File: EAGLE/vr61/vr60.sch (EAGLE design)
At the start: 228 parts, among them IC1 MC74VHC1G50, J6 MICROMOD-2222-C

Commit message: wip, logos
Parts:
- removed SG3: MOUNTING-HOLE-WIDE, ts_keyboards:MOUNTING-HOLE-WIDE
- added LOGO1: OSHW-LOGOL, random_logos:OSHW-LOGOL
- added U$5: SPARKFUN_LOGO0.2, random_logos:SPARKFUN_LOGO0.2
- SG1, SG4: value MOUNTING-HOLE-VWIDE -> MOUNTING-HOLE-VWIDEEDGE-CUT; device ts_keyboards:MOUNTING-HOLE-VWIDE -> ts_keyboards:MOUNTING-HOLE-VWIDEEDGE-CUT
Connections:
- removed net SG3: SG3.P$1
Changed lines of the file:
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@@
 <part name="U$3" library="ts_keyboards" deviceset="ESD_SRV05-4" device=""/>
 <part name="SC1" library="ts_keyboards" deviceset="MOUNTING-HOLE" device=""/>
-<part name="SG1" library="ts_keyboards" deviceset="MOUNTING-HOLE-VWIDE" device=""/>
 <part name="SC2" library="ts_keyboards" deviceset="MOUNTING-HOLE-WIDE" device=""/>
 <part name="U$7" library="ts_keyboards" deviceset="PTC_ASMD1206" device=""/>
@@
 <part name="X1" library="ts_keyboards" deviceset="USB_C" device=""/>
 <part name="GND3" library="ts_custom_nick_nacks" deviceset="GND" device=""/>
-<part name="SG4" library="ts_keyboards" deviceset="MOUNTING-HOLE-VWIDE" device=""/>
 <part name="SA1" library="ts_keyboards" deviceset="MOUNTING-HOLE-WIDE" device=""/>
-<part name="SG3" library="ts_keyboards" deviceset="MOUNTING-HOLE-WIDE" device=""/>
 <part name="SA3" library="ts_keyboards" deviceset="MOUNTING-HOLE-WIDE" device=""/>
 <part name="SA2" library="ts_keyboards" deviceset="MOUNTING-HOLE-WIDE" device=""/>
@@
 <part name="J4" library="SparkFun-Connectors" library_urn="urn:adsk.eagle:library:513" deviceset="CONN_03" device="" package3d_urn="urn:adsk.eagle:package:38063/1"/>
 <part name="U1" library="SparkFun-IC-Power" library_urn="urn:adsk.eagle:library:526" deviceset="V_REG_LM1117" device="SOT223" package3d_urn="urn:adsk.eagle:package:39069/1"/>
+<part name="SG1" library="ts_keyboards" deviceset="MOUNTING-HOLE-VWIDE" device="EDGE-CUT"/>
+<part name="SG4" library="ts_keyboards" deviceset="MOUNTING-HOLE-VWIDE" device="EDGE-CUT"/>
+<part name="LOGO1" library="random_logos" deviceset="OSHW-LOGO" device="L"/>
+<part name="U$5" library="random_logos" deviceset="SPARKFUN_LOGO" device="0.2"/>
 </parts>
 <sheets>
@@
 <instance part="U$3" gate="G$1" x="71.12" y="149.86" smashed="yes" rot="R90"/>
 <instance part="SC1" gate="G$1" x="233.68" y="33.02" smashed="yes"/>
-<instance part="SG1" gate="G$1" x="241.3" y="33.02" smashed="yes"/>
 <instance part="SC2" gate="G$1" x="236.22" y="33.02" smashed="yes"/>
 <instance part="U$7" gate="G$1" x="101.6" y="165.1" smashed="yes">
@@
 <attribute name="VALUE" x="170.18" y="3.048" size="1.778" layer="96" align="top-center"/>
 </instance>
-<instance part="SG4" gate="G$1" x="248.92" y="33.02" smashed="yes"/>
 <instance part="SA1" gate="G$1" x="254" y="33.02" smashed="yes"/>
-<instance part="SG3" gate="G$1" x="246.38" y="33.02" smashed="yes"/>
 <instance part="SA3" gate="G$1" x="259.08" y="33.02" smashed="yes"/>
 <instance part="SA2" gate="G$1" x="256.54" y="33.02" smashed="yes"/>
@@
 <attribute name="VALUE" x="88.9" y="53.34" size="1.778" layer="96" font="vector"/>
 </instance>
+<instance part="SG1" gate="G$1" x="241.3" y="35.56" smashed="yes"/>
+<instance part="SG4" gate="G$1" x="248.92" y="35.56" smashed="yes"/>
+<instance part="LOGO1" gate="G$1" x="210.82" y="22.86" smashed="yes"/>
+<instance part="U$5" gate="G$1" x="210.82" y="25.4" smashed="yes"/>
 </instances>
 <busses>
@@
 <segment>
 <label x="246.38" y="30.48" size="1.778" layer="95" rot="R270"/>
-<pinref part="SG3" gate="G$1" pin="P$1"/>
-<wire x1="246.38" y1="31.496" x2="246.38" y2="30.48" width="0.1524" layer="91"/>
+<wire x1="246.38" y1="34.036" x2="246.38" y2="30.48" width="0.1524" layer="91"/>
 </segment>
 </net>
@@
 <segment>
 <label x="241.3" y="30.48" size="1.778" layer="95" rot="R270"/>
+<wire x1="241.3" y1="34.036" x2="241.3" y2="30.48" width="0.1524" layer="91"/>
 <pinref part="SG1" gate="G$1" pin="P$1"/>
-<wire x1="241.3" y1="31.496" x2="241.3" y2="30.48" width="0.1524" layer="91"/>
 </segment>
 </net>
@@
 <segment>
 <label x="248.92" y="30.48" size="1.778" layer="95" rot="R270"/>
+<wire x1="248.92" y1="34.036" x2="248.92" y2="30.48" width="0.1524" layer="91"/>
 <pinref part="SG4" gate="G$1" pin="P$1"/>
-<wire x1="248.92" y1="31.496" x2="248.92" y2="30.48" width="0.1524" layer="91"/>
 </segment>
 </net>
 <net name="SG2" class="0">
 <segment>
-<wire x1="243.84" y1="30.48" x2="243.84" y2="33.02" width="0.1524" layer="91"/>
+<wire x1="243.84" y1="30.48" x2="243.84" y2="34.036" width="0.1524" layer="91"/>
 <label x="243.84" y="30.48" size="1.778" layer="95" rot="R270"/>
 </segment>

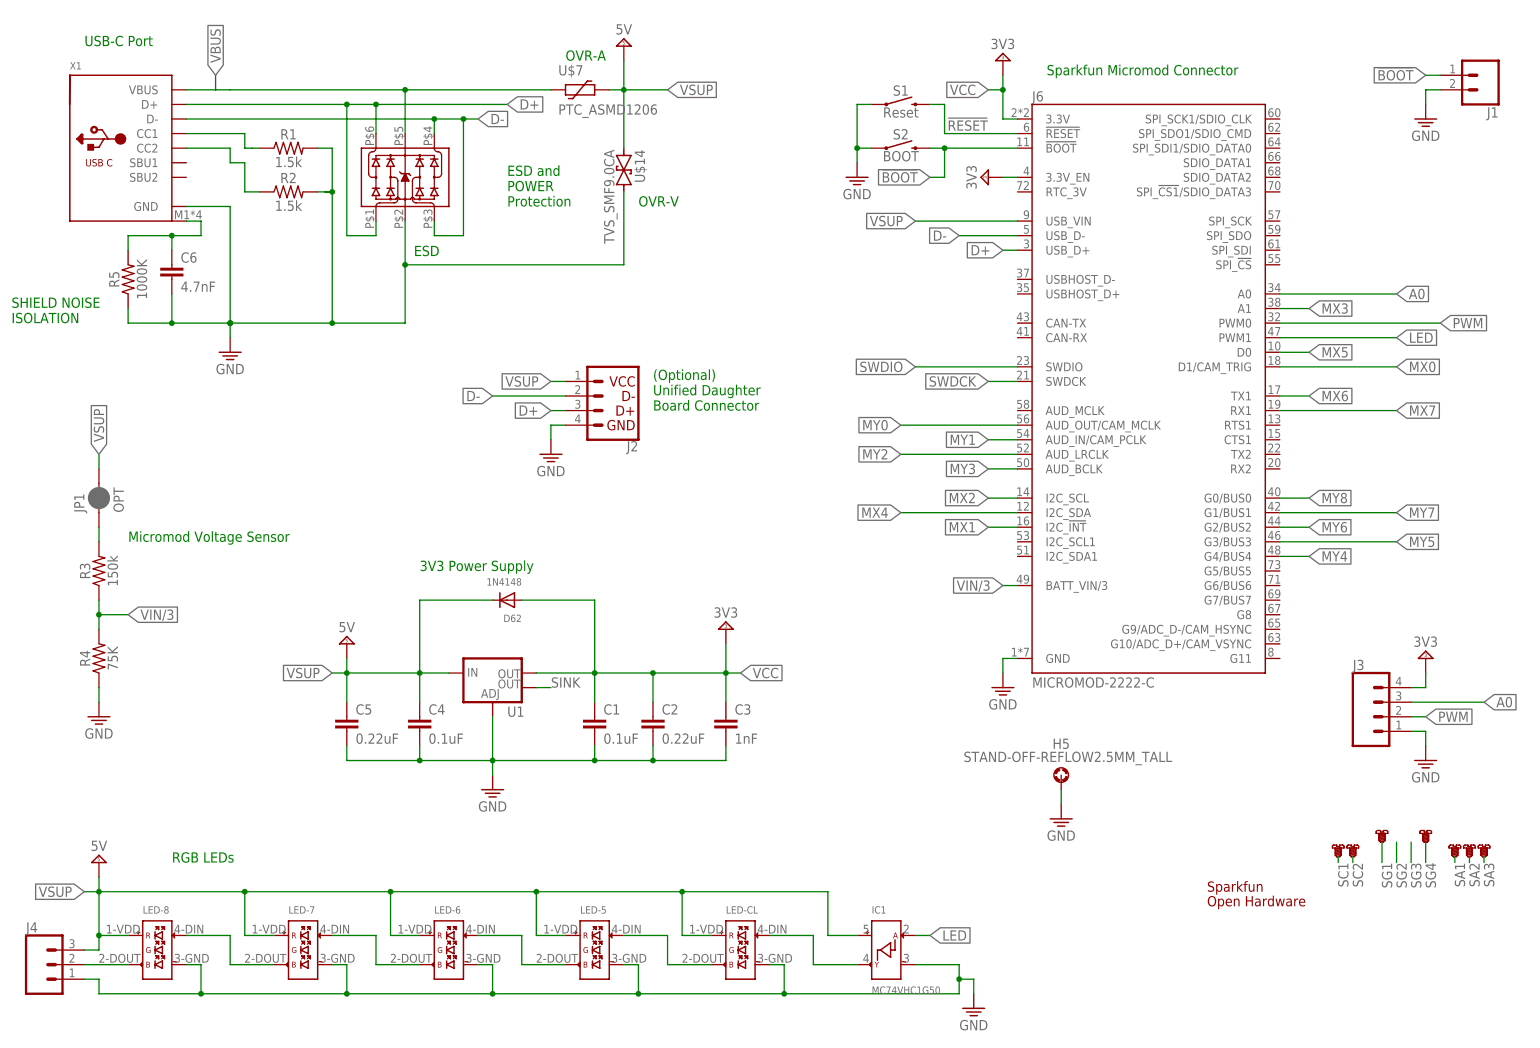
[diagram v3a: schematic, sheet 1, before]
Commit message: logos and text
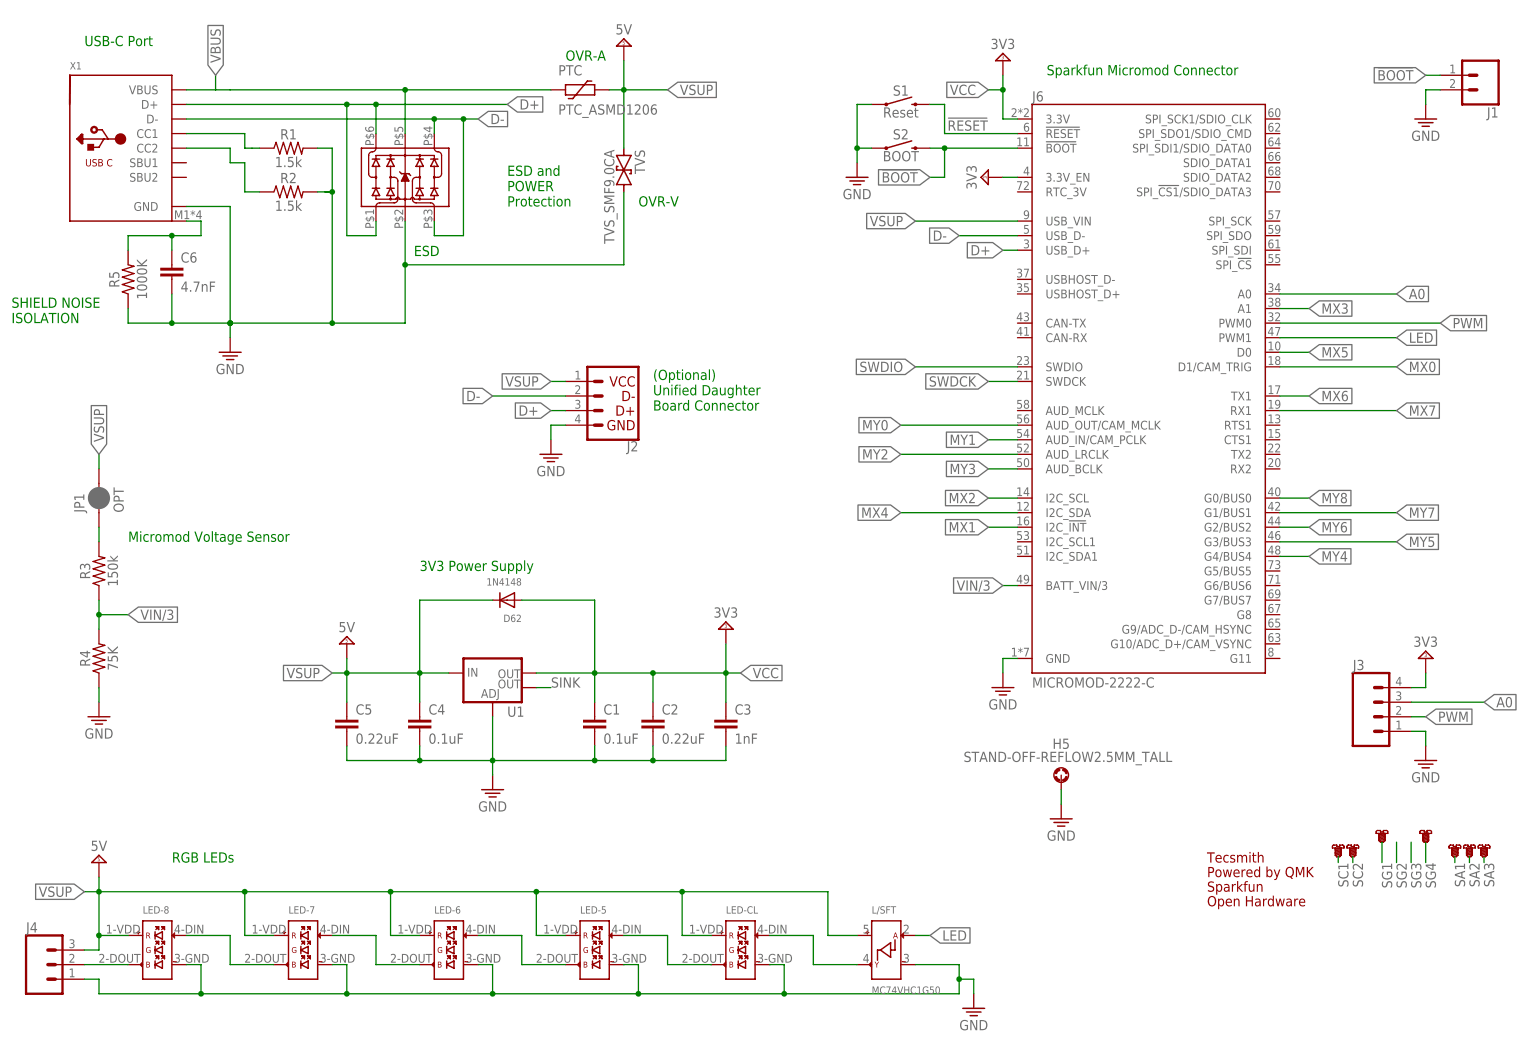
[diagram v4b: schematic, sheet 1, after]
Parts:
- added U$6: QMK_LOGO, random_logos:QMK_LOGO
- added U$8: TECSMITH-LOGOLONG, random_logos:TECSMITH-LOGOLONG
- renumbered IC1 to L/SFT, U$14 to TVS, U$3 to ESD, U$7 to PTC
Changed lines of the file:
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@@
 <part name="GND1" library="ts_custom_nick_nacks" deviceset="GND" device=""/>
 <part name="GND2" library="ts_custom_nick_nacks" deviceset="GND" device=""/>
-<part name="U$3" library="ts_keyboards" deviceset="ESD_SRV05-4" device=""/>
+<part name="ESD" library="ts_keyboards" deviceset="ESD_SRV05-4" device=""/>
 <part name="SC1" library="ts_keyboards" deviceset="MOUNTING-HOLE" device=""/>
 <part name="SC2" library="ts_keyboards" deviceset="MOUNTING-HOLE-WIDE" device=""/>
-<part name="U$7" library="ts_keyboards" deviceset="PTC_ASMD1206" device=""/>
+<part name="PTC" library="ts_keyboards" deviceset="PTC_ASMD1206" device=""/>
 <part name="LED-CL" library="ts_keyboards" deviceset="SK6812-E-REVERSE" device=""/>
 <part name="LED-5" library="ts_keyboards" deviceset="SK6812-E-REVERSE" device=""/>
@@
 <part name="LED-7" library="ts_keyboards" deviceset="SK6812-E-REVERSE" device=""/>
 <part name="LED-8" library="ts_keyboards" deviceset="SK6812-E-REVERSE" device=""/>
-<part name="U$14" library="ts_keyboards" deviceset="TVS_SMF9.0CA" device=""/>
+<part name="TVS" library="ts_keyboards" deviceset="TVS_SMF9.0CA" device=""/>
 <part name="X1" library="ts_keyboards" deviceset="USB_C" device=""/>
 <part name="GND3" library="ts_custom_nick_nacks" deviceset="GND" device=""/>
@@
 <part name="R5" library="SparkFun-Resistors" library_urn="urn:adsk.eagle:library:532" deviceset="75KOHM" device="-0603-1/10W-1%" package3d_urn="urn:adsk.eagle:package:39650/1" value="1000K"/>
 <part name="C6" library="SparkFun-Capacitors" library_urn="urn:adsk.eagle:library:510" deviceset="0.1UF" device="-0603-25V-5%" package3d_urn="urn:adsk.eagle:package:37414/1" value="4.7nF"/>
-<part name="IC1" library="ts_keyboards" deviceset="MC74VHC1G50" device=""/>
+<part name="L/SFT" library="ts_keyboards" deviceset="MC74VHC1G50" device=""/>
 <part name="JP1" library="SparkFun-Jumpers" library_urn="urn:adsk.eagle:library:528" deviceset="JUMPER-SMT_2_NC_PASTE" device="_NO-SILK" package3d_urn="urn:adsk.eagle:package:39283/1" value="OPT"/>
 <part name="J1" library="SparkFun-Connectors" library_urn="urn:adsk.eagle:library:513" deviceset="CONN_02" device="" package3d_urn="urn:adsk.eagle:package:38039/1"/>
@@
 <part name="LOGO1" library="random_logos" deviceset="OSHW-LOGO" device="L"/>
 <part name="U$5" library="random_logos" deviceset="SPARKFUN_LOGO" device="0.2"/>
+<part name="U$6" library="random_logos" deviceset="QMK_LOGO" device=""/>
+<part name="U$8" library="random_logos" deviceset="TECSMITH-LOGO" device="LONG"/>
 </parts>
 <sheets>
@@
 <attribute name="VALUE" x="185.42" y="36.068" size="1.778" layer="96" align="top-center"/>
 </instance>
-<instance part="U$3" gate="G$1" x="71.12" y="149.86" smashed="yes" rot="R90"/>
+<instance part="ESD" gate="G$1" x="71.12" y="149.86" smashed="yes" rot="R90"/>
 <instance part="SC1" gate="G$1" x="233.68" y="33.02" smashed="yes"/>
 <instance part="SC2" gate="G$1" x="236.22" y="33.02" smashed="yes"/>
-<instance part="U$7" gate="G$1" x="101.6" y="165.1" smashed="yes">
+<instance part="PTC" gate="G$1" x="101.6" y="165.1" smashed="yes">
 <attribute name="NAME" x="97.79" y="167.6146" size="1.778" layer="95"/>
 <attribute name="VALUE" x="97.79" y="160.782" size="1.778" layer="96"/>
@@
 <attribute name="NAME" x="25.4" y="21.59" size="1.27" layer="95"/>
 </instance>
-<instance part="U$14" gate="G$1" x="109.22" y="152.4" smashed="yes" rot="R270">
+<instance part="TVS" gate="G$1" x="109.22" y="152.4" smashed="yes" rot="R270">
 <attribute name="NAME" x="111.125" y="154.686" size="1.778" layer="95" rot="R270"/>
 <attribute name="VALUE" x="105.791" y="154.686" size="1.778" layer="96" rot="R270"/>
@@
 <attribute name="VALUE" x="32.004" y="129.921" size="1.778" layer="96" font="vector"/>
 </instance>
-<instance part="IC1" gate="G$1" x="154.94" y="15.24" smashed="yes">
+<instance part="L/SFT" gate="G$1" x="154.94" y="15.24" smashed="yes">
 <attribute name="NAME" x="152.4" y="21.59" size="1.27" layer="95"/>
 <attribute name="VALUE" x="152.4" y="7.62" size="1.27" layer="96"/>
@@
 <instance part="LOGO1" gate="G$1" x="210.82" y="22.86" smashed="yes"/>
 <instance part="U$5" gate="G$1" x="210.82" y="25.4" smashed="yes"/>
+<instance part="U$6" gate="G$1" x="210.82" y="27.94" smashed="yes"/>
+<instance part="U$8" gate="G$1" x="210.82" y="30.48" smashed="yes"/>
 </instances>
 <busses>
@@
 <wire x1="58.42" y1="124.46" x2="71.12" y2="124.46" width="0.1524" layer="91"/>
 <junction x="58.42" y="124.46"/>
-<pinref part="U$3" gate="G$1" pin="P$2"/>
+<pinref part="ESD" gate="G$1" pin="P$2"/>
 <wire x1="71.12" y1="134.62" x2="71.12" y2="142.24" width="0.1524" layer="91"/>
 <wire x1="71.12" y1="134.62" x2="109.22" y2="134.62" width="0.1524" layer="91"/>
 <junction x="71.12" y="134.62"/>
-<pinref part="U$14" gate="G$1" pin="2"/>
+<pinref part="TVS" gate="G$1" pin="2"/>
 <wire x1="109.22" y1="134.62" x2="109.22" y2="147.32" width="0.1524" layer="91"/>
 <wire x1="71.12" y1="124.46" x2="71.12" y2="134.62" width="0.1524" layer="91"/>
@@
 <pinref part="GND3" gate="1" pin="GND"/>
 <wire x1="170.18" y1="10.16" x2="170.18" y2="7.62" width="0.1524" layer="91"/>
-<pinref part="IC1" gate="G$1" pin="3_GND"/>
+<pinref part="L/SFT" gate="G$1" pin="3_GND"/>
 <wire x1="160.02" y1="12.7" x2="167.64" y2="12.7" width="0.1524" layer="91"/>
 <wire x1="167.64" y1="12.7" x2="167.64" y2="10.16" width="0.1524" layer="91"/>
@@
 <junction x="119.38" y="25.4"/>
 <wire x1="144.78" y1="25.4" x2="144.78" y2="17.78" width="0.1524" layer="91"/>
-<pinref part="IC1" gate="G$1" pin="5_VCC"/>
+<pinref part="L/SFT" gate="G$1" pin="5_VCC"/>
 <wire x1="144.78" y1="17.78" x2="149.86" y2="17.78" width="0.1524" layer="91"/>
 <pinref part="J4" gate="J$1" pin="3"/>
@@
 <pinref part="U$11" gate="G$1" pin="VCC"/>
 <wire x1="109.22" y1="170.18" x2="109.22" y2="165.1" width="0.1524" layer="91"/>
-<pinref part="U$7" gate="G$1" pin="2"/>
+<pinref part="PTC" gate="G$1" pin="2"/>
 <wire x1="106.68" y1="165.1" x2="109.22" y2="165.1" width="0.1524" layer="91"/>
-<pinref part="U$14" gate="G$1" pin="1"/>
+<pinref part="TVS" gate="G$1" pin="1"/>
 <wire x1="109.22" y1="165.1" x2="116.84" y2="165.1" width="0.1524" layer="91"/>
 <wire x1="109.22" y1="154.94" x2="109.22" y2="165.1" width="0.1524" layer="91"/>
@@
 <pinref part="X1" gate="G$1" pin="D+"/>
 <wire x1="33.02" y1="162.56" x2="60.96" y2="162.56" width="0.1524" layer="91"/>
-<pinref part="U$3" gate="G$1" pin="P$6"/>
+<pinref part="ESD" gate="G$1" pin="P$6"/>
 <wire x1="60.96" y1="162.56" x2="66.04" y2="162.56" width="0.1524" layer="91"/>
 <wire x1="66.04" y1="162.56" x2="88.9" y2="162.56" width="0.1524" layer="91"/>
@@
 <junction x="66.04" y="162.56"/>
 <label x="88.9" y="162.56" size="1.778" layer="95" xref="yes"/>
-<pinref part="U$3" gate="G$1" pin="P$1"/>
+<pinref part="ESD" gate="G$1" pin="P$1"/>
 <wire x1="66.04" y1="142.24" x2="66.04" y2="139.7" width="0.1524" layer="91"/>
 <wire x1="66.04" y1="139.7" x2="60.96" y2="139.7" width="0.1524" layer="91"/>
@@
 <pinref part="X1" gate="G$1" pin="D-"/>
 <wire x1="33.02" y1="160.02" x2="76.2" y2="160.02" width="0.1524" layer="91"/>
-<pinref part="U$3" gate="G$1" pin="P$4"/>
+<pinref part="ESD" gate="G$1" pin="P$4"/>
 <wire x1="76.2" y1="160.02" x2="81.28" y2="160.02" width="0.1524" layer="91"/>
 <wire x1="81.28" y1="160.02" x2="83.82" y2="160.02" width="0.1524" layer="91"/>
@@
 <junction x="76.2" y="160.02"/>
 <label x="83.82" y="160.02" size="1.778" layer="95" xref="yes"/>
-<pinref part="U$3" gate="G$1" pin="P$3"/>
+<pinref part="ESD" gate="G$1" pin="P$3"/>
 <wire x1="76.2" y1="142.24" x2="76.2" y2="139.7" width="0.1524" layer="91"/>
 <wire x1="76.2" y1="139.7" x2="81.28" y2="139.7" width="0.1524" layer="91"/>
@@
 <segment>
 <pinref part="X1" gate="G$1" pin="VBUS"/>
-<pinref part="U$7" gate="G$1" pin="1"/>
+<pinref part="PTC" gate="G$1" pin="1"/>
 <wire x1="33.02" y1="165.1" x2="38.1" y2="165.1" width="0.1524" layer="91"/>
-<pinref part="U$3" gate="G$1" pin="P$5"/>
+<pinref part="ESD" gate="G$1" pin="P$5"/>
 <wire x1="40.64" y1="165.1" x2="71.12" y2="165.1" width="0.1524" layer="91"/>
 <wire x1="71.12" y1="165.1" x2="96.52" y2="165.1" width="0.1524" layer="91"/>
@@
 <wire x1="160.02" y1="17.78" x2="162.56" y2="17.78" width="0.1524" layer="91"/>
 <label x="162.56" y="17.78" size="1.778" layer="95" xref="yes"/>
-<pinref part="IC1" gate="G$1" pin="A_DIN"/>
+<pinref part="L/SFT" gate="G$1" pin="A_DIN"/>
 </segment>
 </net>
@@
 <net name="N$70" class="0">
 <segment>
-<pinref part="IC1" gate="G$1" pin="Y_DOUT"/>
+<pinref part="L/SFT" gate="G$1" pin="Y_DOUT"/>
 <wire x1="149.86" y1="12.7" x2="142.24" y2="12.7" width="0.1524" layer="91"/>
 <wire x1="142.24" y1="12.7" x2="142.24" y2="17.78" width="0.1524" layer="91"/>
